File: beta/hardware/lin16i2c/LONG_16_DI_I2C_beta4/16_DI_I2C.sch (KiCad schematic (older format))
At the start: 105 parts, among them P1 CONN_2, P10 CONN_5, P12 CONN_5, P13 CONN_2, P2 CONN_2, P3 CONN_2, P4 CONN_2, P5 CONN_2, P6 CONN_2, P7 CONN_2, P8 CONN_2, U1 PCF8574, U2 PCF8574

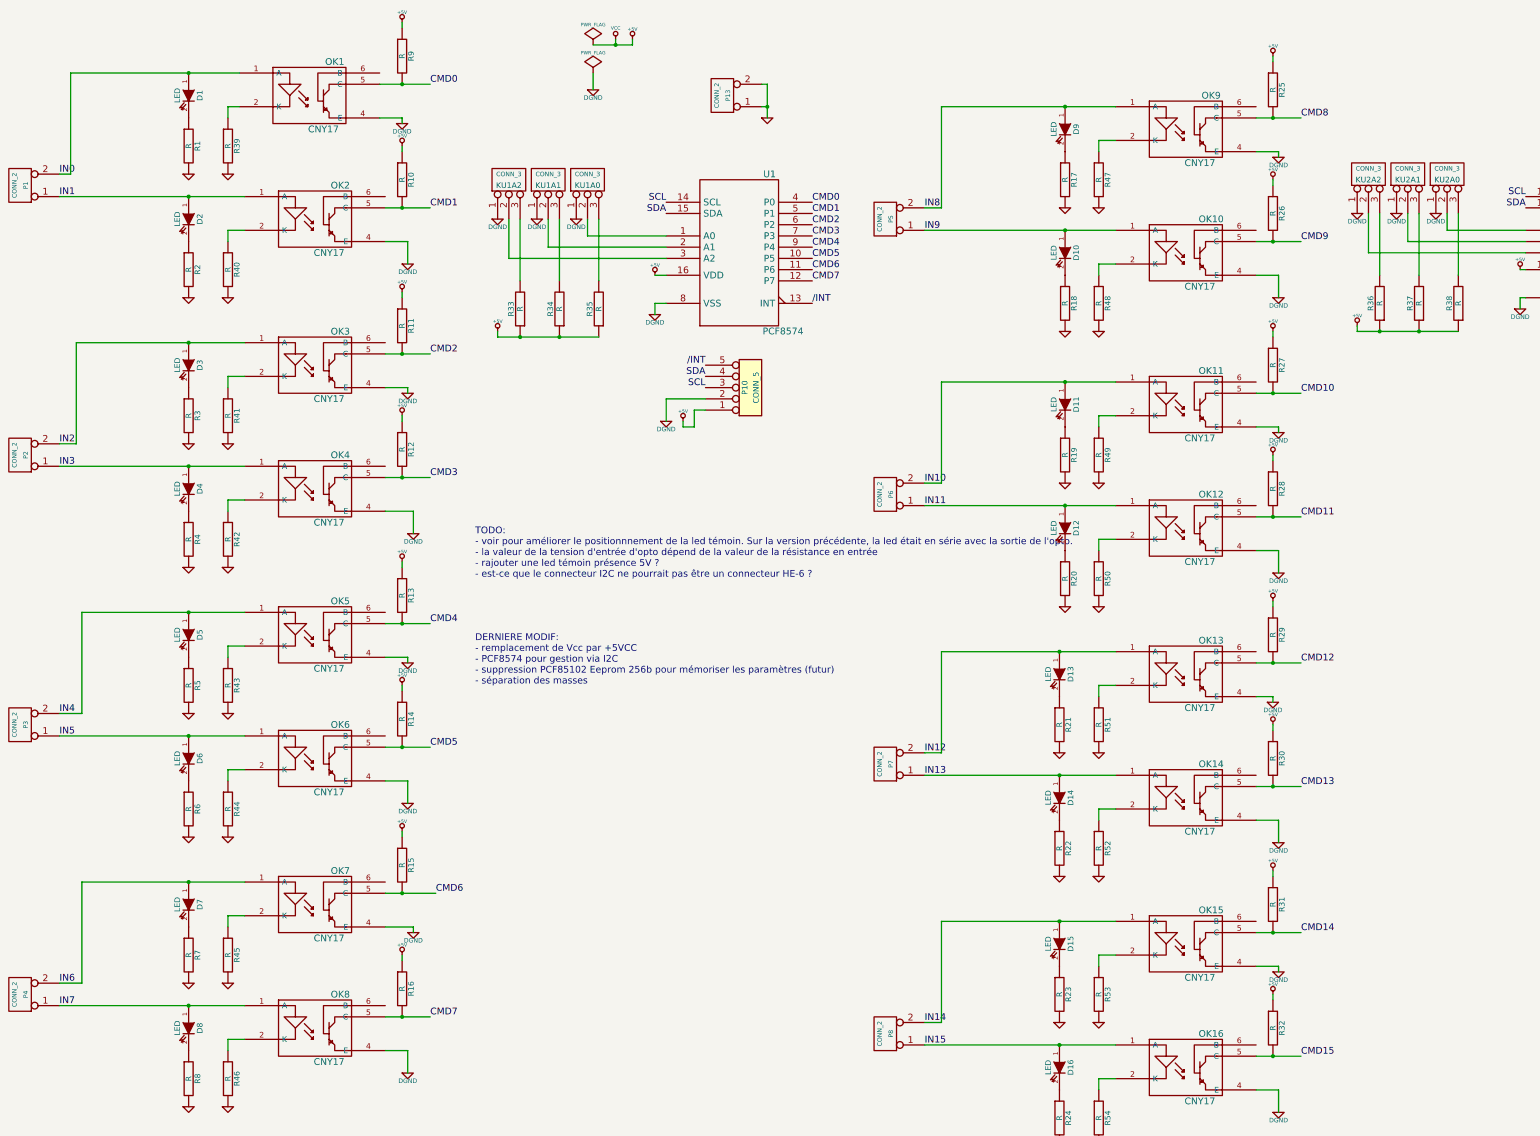
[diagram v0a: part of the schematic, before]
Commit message: Suppression 2 des 3 resistances de pull-up d'adressage Ajout predisposition 2 resistances de pull-up SDA-SCL Ajout led temoin presence VCC
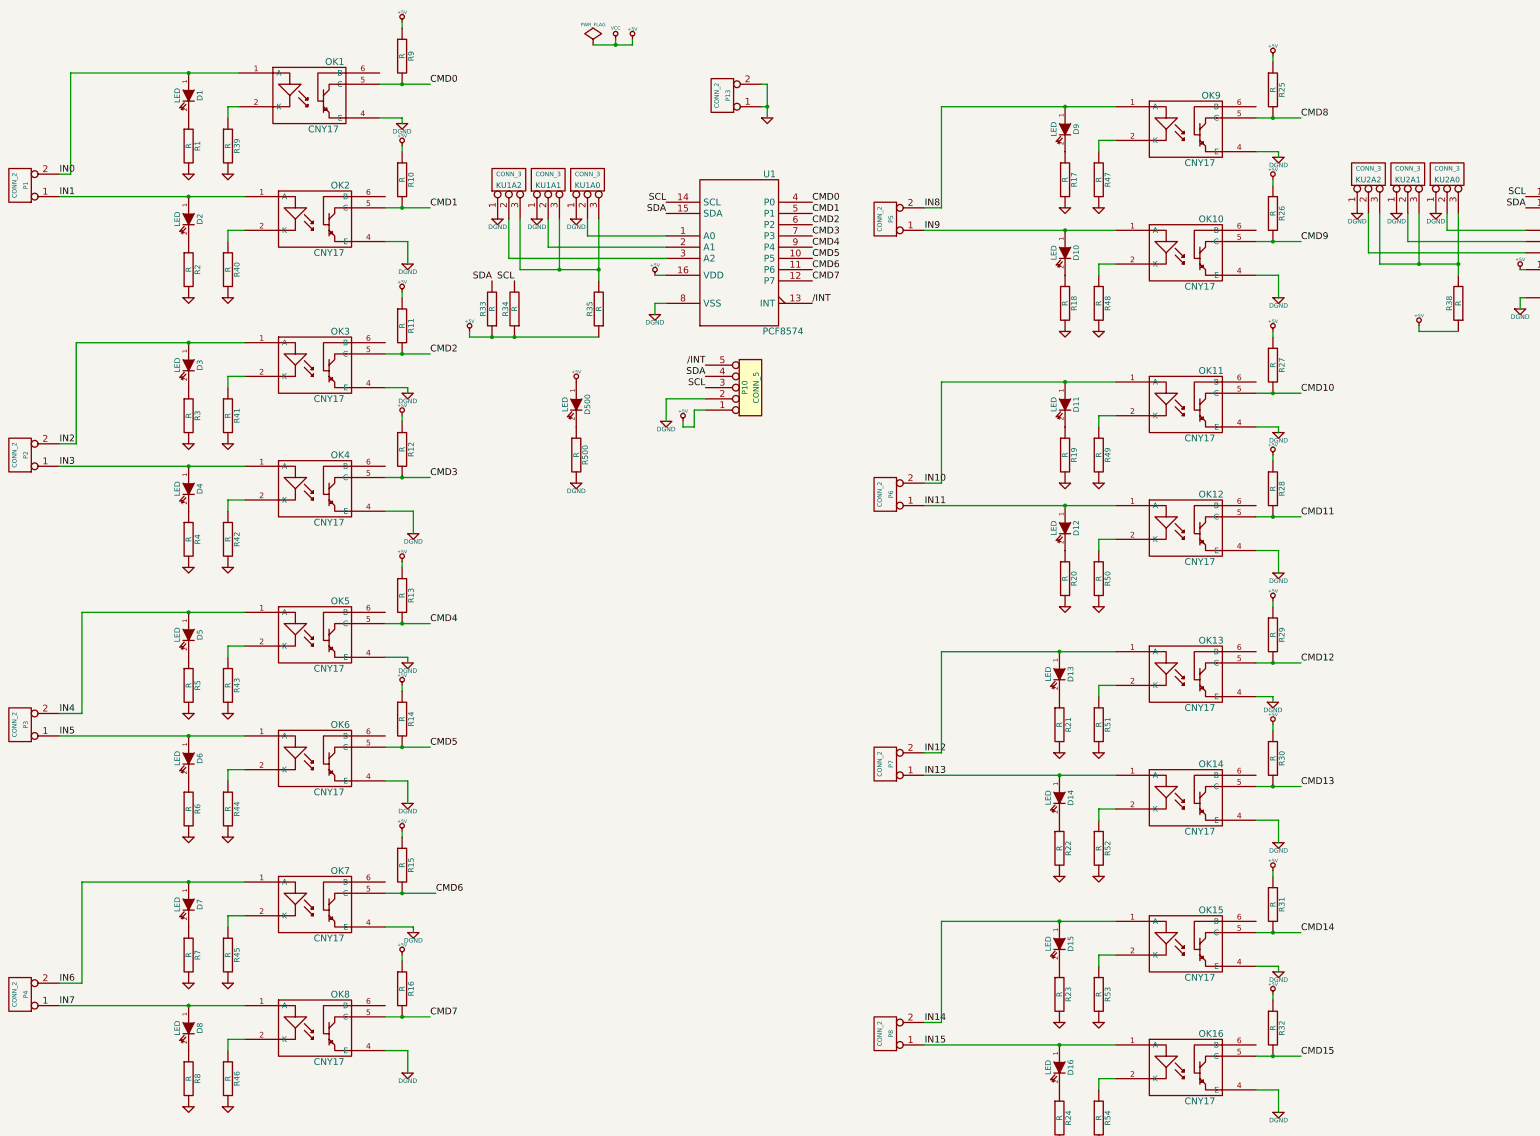
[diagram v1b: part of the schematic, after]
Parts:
- removed R36, R37: R, symbol R
- added D500: LED, symbol LED
- added R500: R, symbol R
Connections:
- net +5V: now also D500.1 (A)
- net DGND: now also R500.2
- net SCL: now also R34.2
- net SDA: now also R33.2
- net at KU1A2.3 (P3): now also KU1A0.3 (P3), KU1A1.3 (P3), R35.2; no longer R33.2
- net at KU2A1.3 (P3): now also KU2A0.3 (P3), KU2A2.3 (P3), R38.2
- new net: D500.2 (K), R500.1
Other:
- note removed: "DERNIERE MODIF:\n- remplacement de Vcc par +5VCC\n- PCF8574 pour gestion via I2C\n- suppression PCF85102 Eeprom 256b pour mémoriser les paramètres (futur)\n- séparation des masses"
- note removed: "TODO:\n- voir pour améliorer le positionnnement de la led témoin. Sur la version précédente, la led était en série avec la sortie de l'opto.\n- la valeur de la tension d'entrée d'opto dépend de la valeur de la résistance en entrée\n- rajouter une led témoin présence 5V ?\n- est-ce que le connecteur I2C ne pourrait pas être un connecteur HE-6 ?"
- moved on the sheet: R33, R34
